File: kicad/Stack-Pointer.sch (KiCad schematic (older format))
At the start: 38 parts, among them U137 74LS245, U138 74LS173, U139 74LS173, U140 74LS245, U141 74LS173, U142 74LS173

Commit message: Finish todo list
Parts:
- removed D100, D101, D86, D87, D88, D89, D90, D91, D92, D93, D94, D95, D96, D97, D98, D99: LED, symbol Device:LED
- removed R100, R101, R102, R103, R104, R105, R106, R107, R92, R93, R94, R95, R96, R97, R98, R99: 220, symbol Device:R
- removed U137, U140: 74LS245, symbol 74xx:74LS245
- removed U138, U139, U141, U142: 74LS173, symbol 74xx:74LS173
- added U? (x2): 74LS245, symbol 74xx:74LS245
- added U? (x4): 74LS191, symbol 74xx:74LS191
- added U? (x8): 74LS86, symbol 74xx:74LS86
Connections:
- net BUS_0: now also U?.15 (P0), U?.18 (B0)
- net BUS_1: now also U?.1 (P1), U?.17 (B1)
- net BUS_10: now also U?.10 (P2), U?.16 (B2)
- net BUS_11: now also U?.15 (B3), U?.9 (P3)
- net BUS_12: now also U?.14 (B4), U?.15 (P0)
- net BUS_13: now also U?.1 (P1), U?.13 (B5)
- net BUS_14: now also U?.10 (P2), U?.12 (B6)
- net BUS_15: now also U?.11 (B7), U?.9 (P3)
- net BUS_2: now also U?.10 (P2), U?.16 (B2)
- net BUS_3: now also U?.15 (B3), U?.9 (P3)
- net BUS_4: now also U?.14 (B4), U?.15 (P0)
- net BUS_5: now also U?.1 (P1), U?.13 (B5)
- net BUS_6: now also U?.10 (P2), U?.12 (B6)
- net BUS_7: now also U?.11 (B7), U?.9 (P3)
- net BUS_8: now also U?.15 (P0), U?.18 (B0)
- net BUS_9: now also U?.1 (P1), U?.17 (B1)
- net CLK: now also U?.2, U?.2, U?.2, U?.2, U?.2, U?.2, U?.2, U?.2
- net CLR: now also U?.14 (Cp), U?.14 (Cp), U?.14 (Cp), U?.14 (Cp)
- net VCC: now also U?.1 (A->B), U?.1 (A->B)
- net ~SPI~: now also U?.11 (Pl), U?.11 (Pl), U?.11 (Pl), U?.11 (Pl)
- net ~SPO~: now also U?.19 (CE), U?.19 (CE)
- new net: U?.2 (A0), U?.3 (Q0) (x2)
- new net: U?.2 (Q1), U?.3 (A1) (x2)
- new net: U?.4 (A2), U?.6 (Q2) (x2)
- new net: U?.5 (A3), U?.7 (Q3) (x2)
- new net: U?.3 (Q0), U?.6 (A4) (x2)
- new net: U?.2 (Q1), U?.7 (A5) (x2)
- new net: U?.6 (Q2), U?.8 (A6) (x2)
- new net: U?.7 (Q3), U?.9 (A7) (x2)
- new net: U?.1, U?.12 (Tc) (x3)
- new net: U?.3, U?.4 (Ce) (x4)
- new net: U?.3, U?.5 (D/U) (x4)
- new net: U?.1, U?.13 (Rc) (x3)
- new net DECSP: U?.1
- new net INCSP: U?.1
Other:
- note removed: "Note: Stack pointer should not reset to 00000 and INC and DEC logic should be added for PUSH and POP instructions. This means switching to 74LS191 or 74LS169"

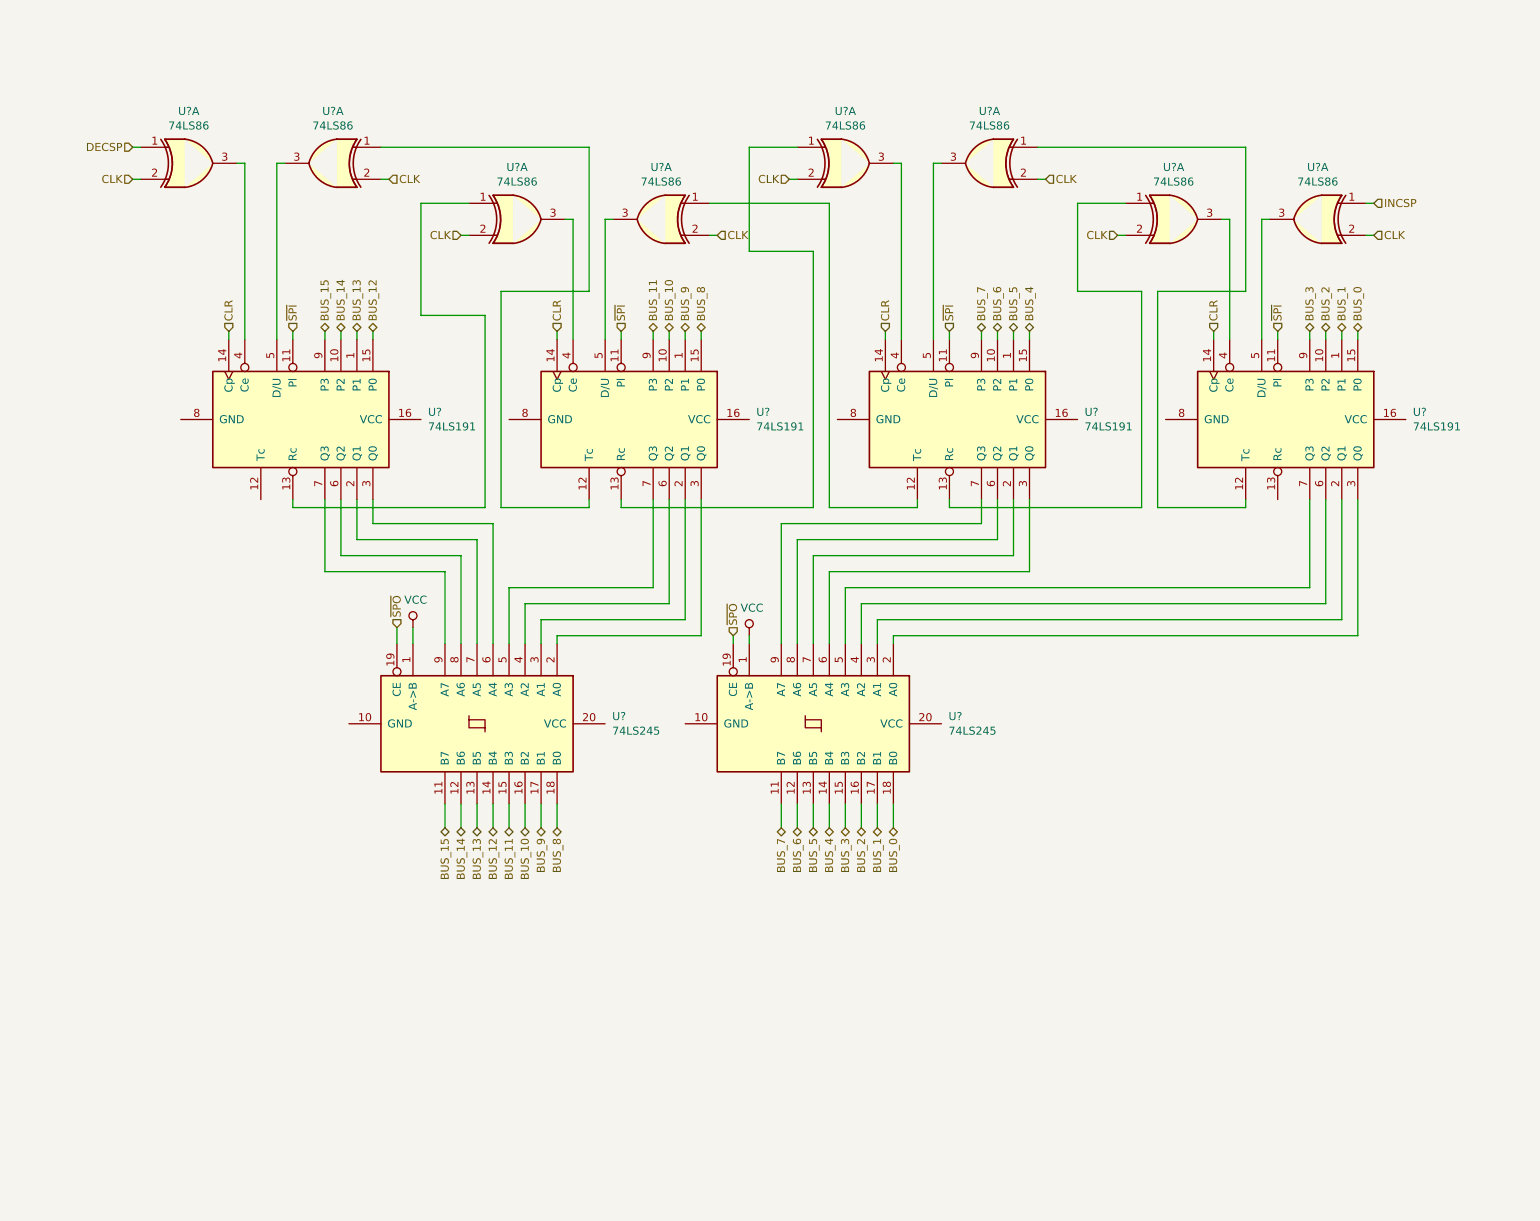
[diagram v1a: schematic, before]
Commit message: Reorganize part references
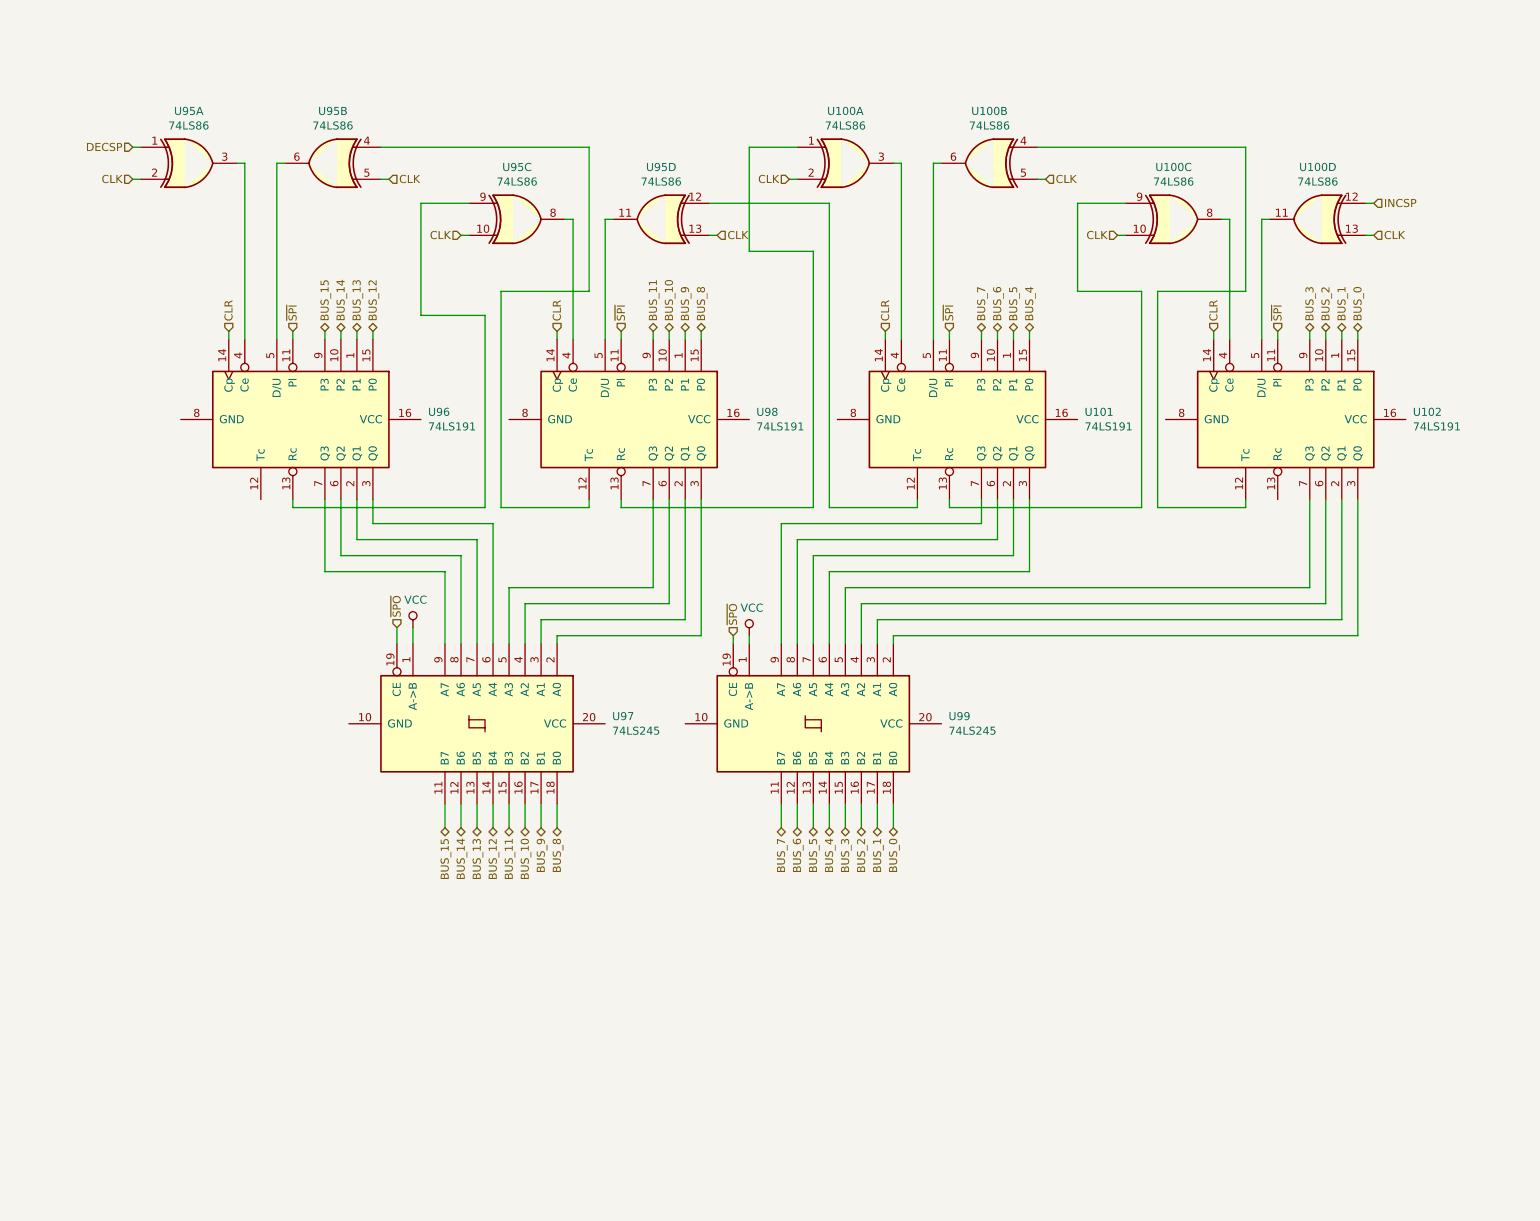
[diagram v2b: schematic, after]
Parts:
- gave numbers to parts that had none: 8
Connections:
- net CLK: now also U100.10, U100.13, U100.5, U95.10, U95.13, U95.5; no longer U100.2, U100.2, U100.2, U95.2, U95.2, U95.2
- net INCSP: now also U100.12; no longer U100.1
- net at U102.12 (Tc): now also U100.4; no longer U100.1
- net at U102.4 (Ce): now also U100.8; no longer U100.3
- net at U102.5 (D/U): now also U100.11; no longer U100.3
- net at U101.13 (Rc): now also U100.9; no longer U100.1
- net at U101.12 (Tc): now also U95.12; no longer U95.1
- net at U101.5 (D/U): now also U100.6; no longer U100.3
- net at U98.12 (Tc): now also U95.4; no longer U95.1
- net at U98.4 (Ce): now also U95.8; no longer U95.3
- net at U98.5 (D/U): now also U95.11; no longer U95.3
- net at U96.13 (Rc): now also U95.9; no longer U95.1
- net at U96.5 (D/U): now also U95.6; no longer U95.3
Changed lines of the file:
@@
 P 3450 4950
 AR Path="/5DA98D6D/5DA9A5CB/5DA57004" Ref="U?"  Part="1"
-AR Path="/5DA98D6D/5DA9A545/5DA57004" Ref="U?"  Part="1"
-F 0 "U?" V 3404 5794 50  0000 L CNN
+AR Path="/5DA98D6D/5DA9A545/5DA57004" Ref="U97"  Part="1"
+F 0 "U97" V 3404 5794 50  0000 L CNN
 F 1 "74LS245" V 3495 5794 50  0000 L CNN
 F 2 "" H 3450 4950 50  0001 C CNN
@@
 P 5550 4950
 AR Path="/5DA98D6D/5DA9A5CB/5DA5700A" Ref="U?"  Part="1"
-AR Path="/5DA98D6D/5DA9A545/5DA5700A" Ref="U?"  Part="1"
-F 0 "U?" V 5504 5794 50  0000 L CNN
+AR Path="/5DA98D6D/5DA9A545/5DA5700A" Ref="U99"  Part="1"
+F 0 "U99" V 5504 5794 50  0000 L CNN
 F 1 "74LS245" V 5595 5794 50  0000 L CNN
 F 2 "" H 5550 4950 50  0001 C CNN
@@
 	8050 2500 8050 2550
 $Comp
-L 74xx:74LS191 U?
+L 74xx:74LS191 U102
 U 1 1 5DB14F60
 P 8550 3050
-F 0 "U?" V 8504 3794 50  0000 L CNN
+F 0 "U102" V 8504 3794 50  0000 L CNN
 F 1 "74LS191" V 8595 3794 50  0000 L CNN
 F 2 "" H 8550 3050 50  0001 C CNN
@@
 $EndComp
 $Comp
-L 74xx:74LS191 U?
+L 74xx:74LS191 U101
 U 1 1 5DB86D50
 P 6500 3050
-F 0 "U?" V 6454 3794 50  0000 L CNN
+F 0 "U101" V 6454 3794 50  0000 L CNN
 F 1 "74LS191" V 6545 3794 50  0000 L CNN
 F 2 "" H 6500 3050 50  0001 C CNN
@@
 $EndComp
 $Comp
-L 74xx:74LS86 U?
-U 1 1 5DBE960D
+L 74xx:74LS86 U100
+U 4 1 5DBE960D
 P 8700 1800
-F 0 "U?" H 8700 2125 50  0000 C CNN
+F 0 "U100" H 8700 2125 50  0000 C CNN
 F 1 "74LS86" H 8700 2034 50  0000 C CNN
 F 2 "" H 8700 1800 50  0001 C CNN
 F 3 "74xx/74ls86.pdf" H 8700 1800 50  0001 C CNN
-	1    8700 1800
+	4    8700 1800
 	-1   0    0    -1
 $EndComp
@@
 	8350 1800 8400 1800
 $Comp
-L 74xx:74LS86 U?
-U 1 1 5DB27703
+L 74xx:74LS86 U100
+U 3 1 5DB27703
 P 7800 1800
-F 0 "U?" H 7800 2125 50  0000 C CNN
+F 0 "U100" H 7800 2125 50  0000 C CNN
 F 1 "74LS86" H 7800 2034 50  0000 C CNN
 F 2 "" H 7800 1800 50  0001 C CNN
 F 3 "74xx/74ls86.pdf" H 7800 1800 50  0001 C CNN
-	1    7800 1800
+	3    7800 1800
 	1    0    0    -1
 $EndComp
@@
 	7450 1900 7500 1900
 $Comp
-L 74xx:74LS86 U?
-U 1 1 5DC447D6
+L 74xx:74LS86 U100
+U 2 1 5DC447D6
 P 6650 1450
-F 0 "U?" H 6650 1775 50  0000 C CNN
+F 0 "U100" H 6650 1775 50  0000 C CNN
 F 1 "74LS86" H 6650 1684 50  0000 C CNN
 F 2 "" H 6650 1450 50  0001 C CNN
 F 3 "74xx/74ls86.pdf" H 6650 1450 50  0001 C CNN
-	1    6650 1450
+	2    6650 1450
 	-1   0    0    -1
 $EndComp
@@
 	6300 1450 6350 1450
 $Comp
-L 74xx:74LS86 U?
+L 74xx:74LS86 U100
 U 1 1 5DC447DF
 P 5750 1450
-F 0 "U?" H 5750 1775 50  0000 C CNN
+F 0 "U100" H 5750 1775 50  0000 C CNN
 F 1 "74LS86" H 5750 1684 50  0000 C CNN
 F 2 "" H 5750 1450 50  0001 C CNN
@@
 	8250 3600 7700 3600
 $Comp
-L 74xx:74LS191 U?
+L 74xx:74LS191 U98
 U 1 1 5DCAEED0
 P 4450 3050
-F 0 "U?" V 4404 3794 50  0000 L CNN
+F 0 "U98" V 4404 3794 50  0000 L CNN
 F 1 "74LS191" V 4495 3794 50  0000 L CNN
 F 2 "" H 4450 3050 50  0001 C CNN
@@
 	5150 1350 5450 1350
 $Comp
-L 74xx:74LS86 U?
-U 1 1 5DD0CA8A
+L 74xx:74LS86 U95
+U 4 1 5DD0CA8A
 P 4600 1800
-F 0 "U?" H 4600 2125 50  0000 C CNN
+F 0 "U95" H 4600 2125 50  0000 C CNN
 F 1 "74LS86" H 4600 2034 50  0000 C CNN
 F 2 "" H 4600 1800 50  0001 C CNN
 F 3 "74xx/74ls86.pdf" H 4600 1800 50  0001 C CNN
-	1    4600 1800
+	4    4600 1800
 	-1   0    0    -1
 $EndComp
@@
 	4250 1800 4300 1800
 $Comp
-L 74xx:74LS86 U?
-U 1 1 5DD0CA93
+L 74xx:74LS86 U95
+U 3 1 5DD0CA93
 P 3700 1800
-F 0 "U?" H 3700 2125 50  0000 C CNN
+F 0 "U95" H 3700 2125 50  0000 C CNN
 F 1 "74LS86" H 3700 2034 50  0000 C CNN
 F 2 "" H 3700 1800 50  0001 C CNN
 F 3 "74xx/74ls86.pdf" H 3700 1800 50  0001 C CNN
-	1    3700 1800
+	3    3700 1800
 	1    0    0    -1
 $EndComp
@@
 	4900 1700 5650 1700
 $Comp
-L 74xx:74LS191 U?
+L 74xx:74LS191 U96
 U 1 1 5DD1D569
 P 2400 3050
-F 0 "U?" V 2354 3794 50  0000 L CNN
+F 0 "U96" V 2354 3794 50  0000 L CNN
 F 1 "74LS191" V 2445 3794 50  0000 L CNN
 F 2 "" H 2400 3050 50  0001 C CNN
@@
 DECSP
 $Comp
-L 74xx:74LS86 U?
-U 1 1 5DD38B59
+L 74xx:74LS86 U95
+U 2 1 5DD38B59
 P 2550 1450
-F 0 "U?" H 2550 1775 50  0000 C CNN
+F 0 "U95" H 2550 1775 50  0000 C CNN
 F 1 "74LS86" H 2550 1684 50  0000 C CNN
 F 2 "" H 2550 1450 50  0001 C CNN
 F 3 "74xx/74ls86.pdf" H 2550 1450 50  0001 C CNN
-	1    2550 1450
+	2    2550 1450
 	-1   0    0    -1
 $EndComp
@@
 	1300 1350 1350 1350
 $Comp
-L 74xx:74LS86 U?
+L 74xx:74LS86 U95
 U 1 1 5DD38B62
 P 1650 1450
-F 0 "U?" H 1650 1775 50  0000 C CNN
+F 0 "U95" H 1650 1775 50  0000 C CNN
 F 1 "74LS86" H 1650 1684 50  0000 C CNN
 F 2 "" H 1650 1450 50  0001 C CNN

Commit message: Up to v1.0 and plot
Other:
- moved on the sheet: U100A, U100B, U100C, U100D, U101, U102, U95A, U95B, U95C, U95D, U96, U97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
